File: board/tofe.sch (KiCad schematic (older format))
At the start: 6 parts, among them P301 TOFE-8X, U301 24AA01/24LC01B

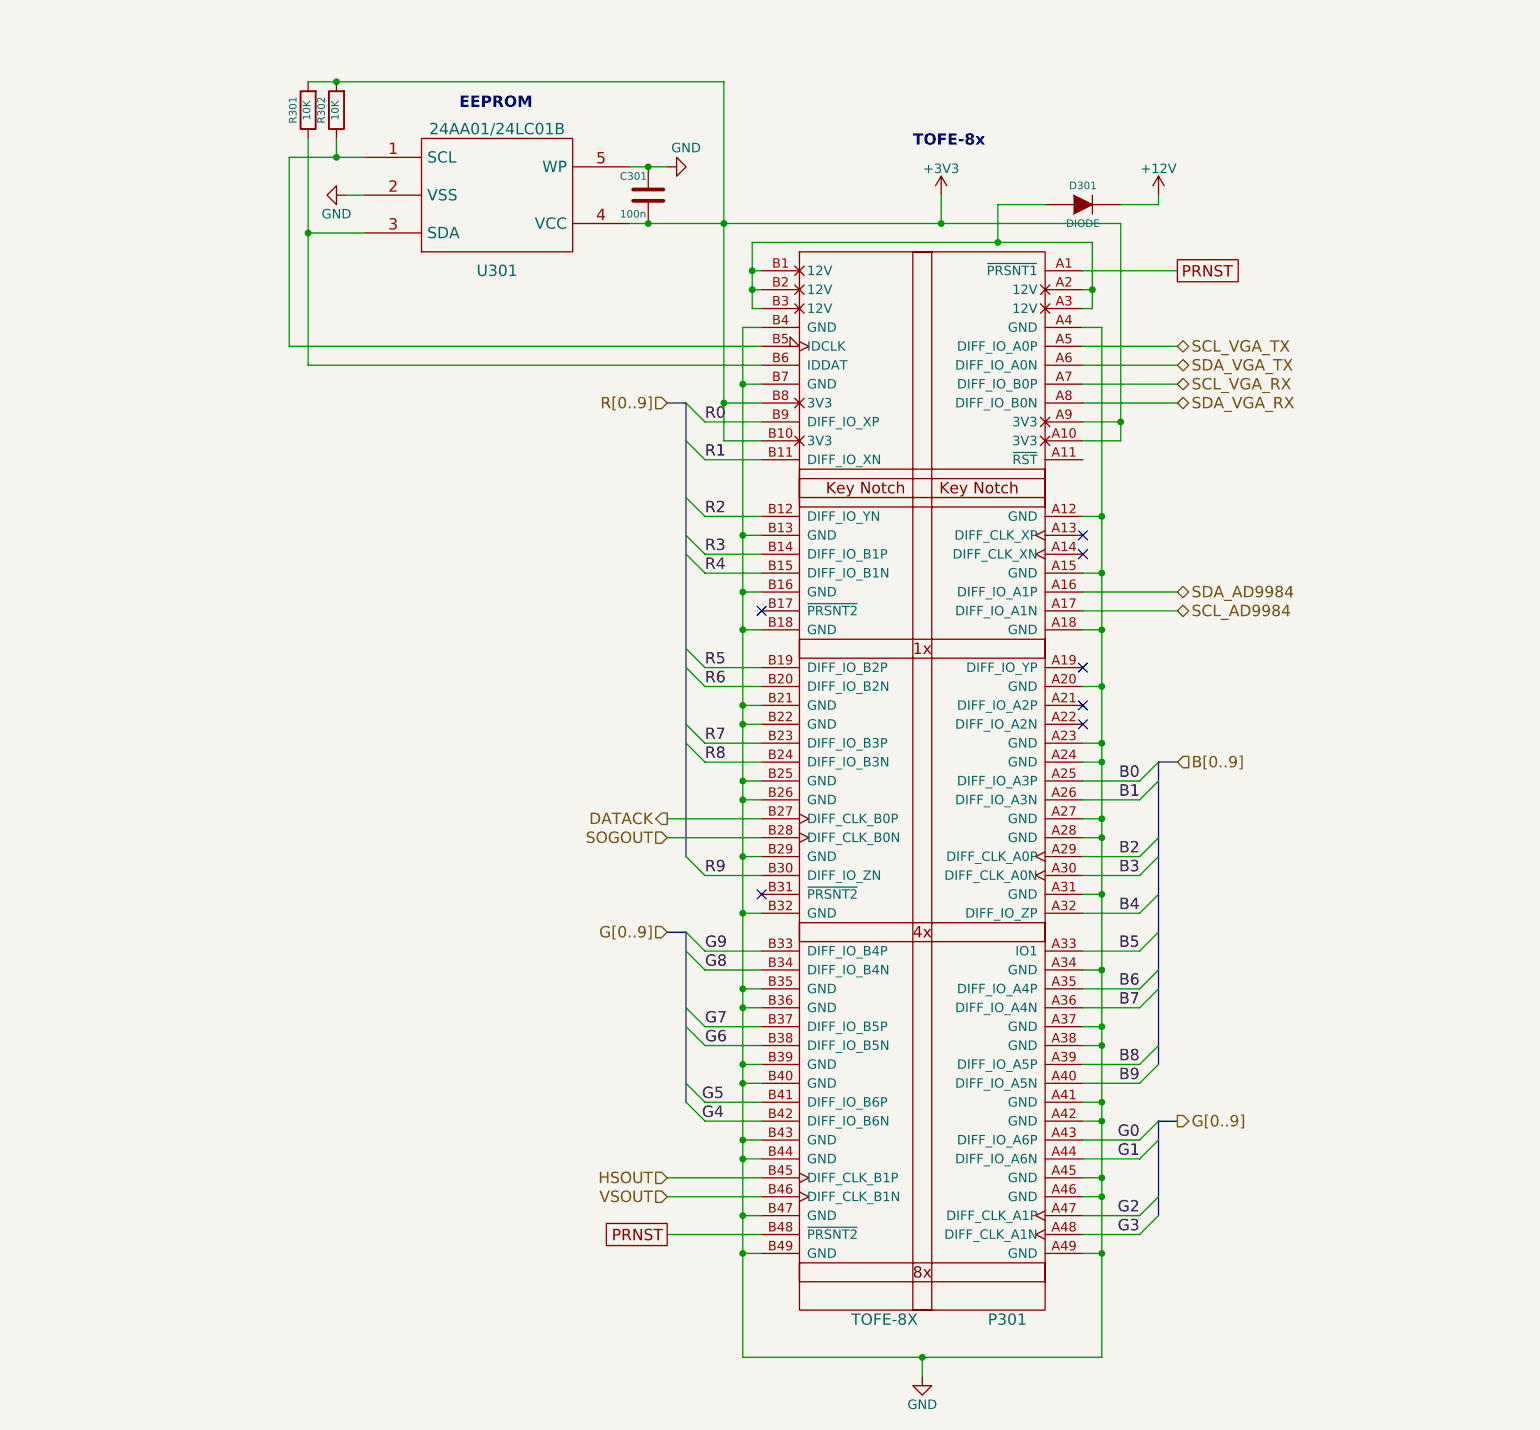
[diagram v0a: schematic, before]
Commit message: Add jumper for EEPROM WP and breakout unused pins to header that can jumper to LEDs
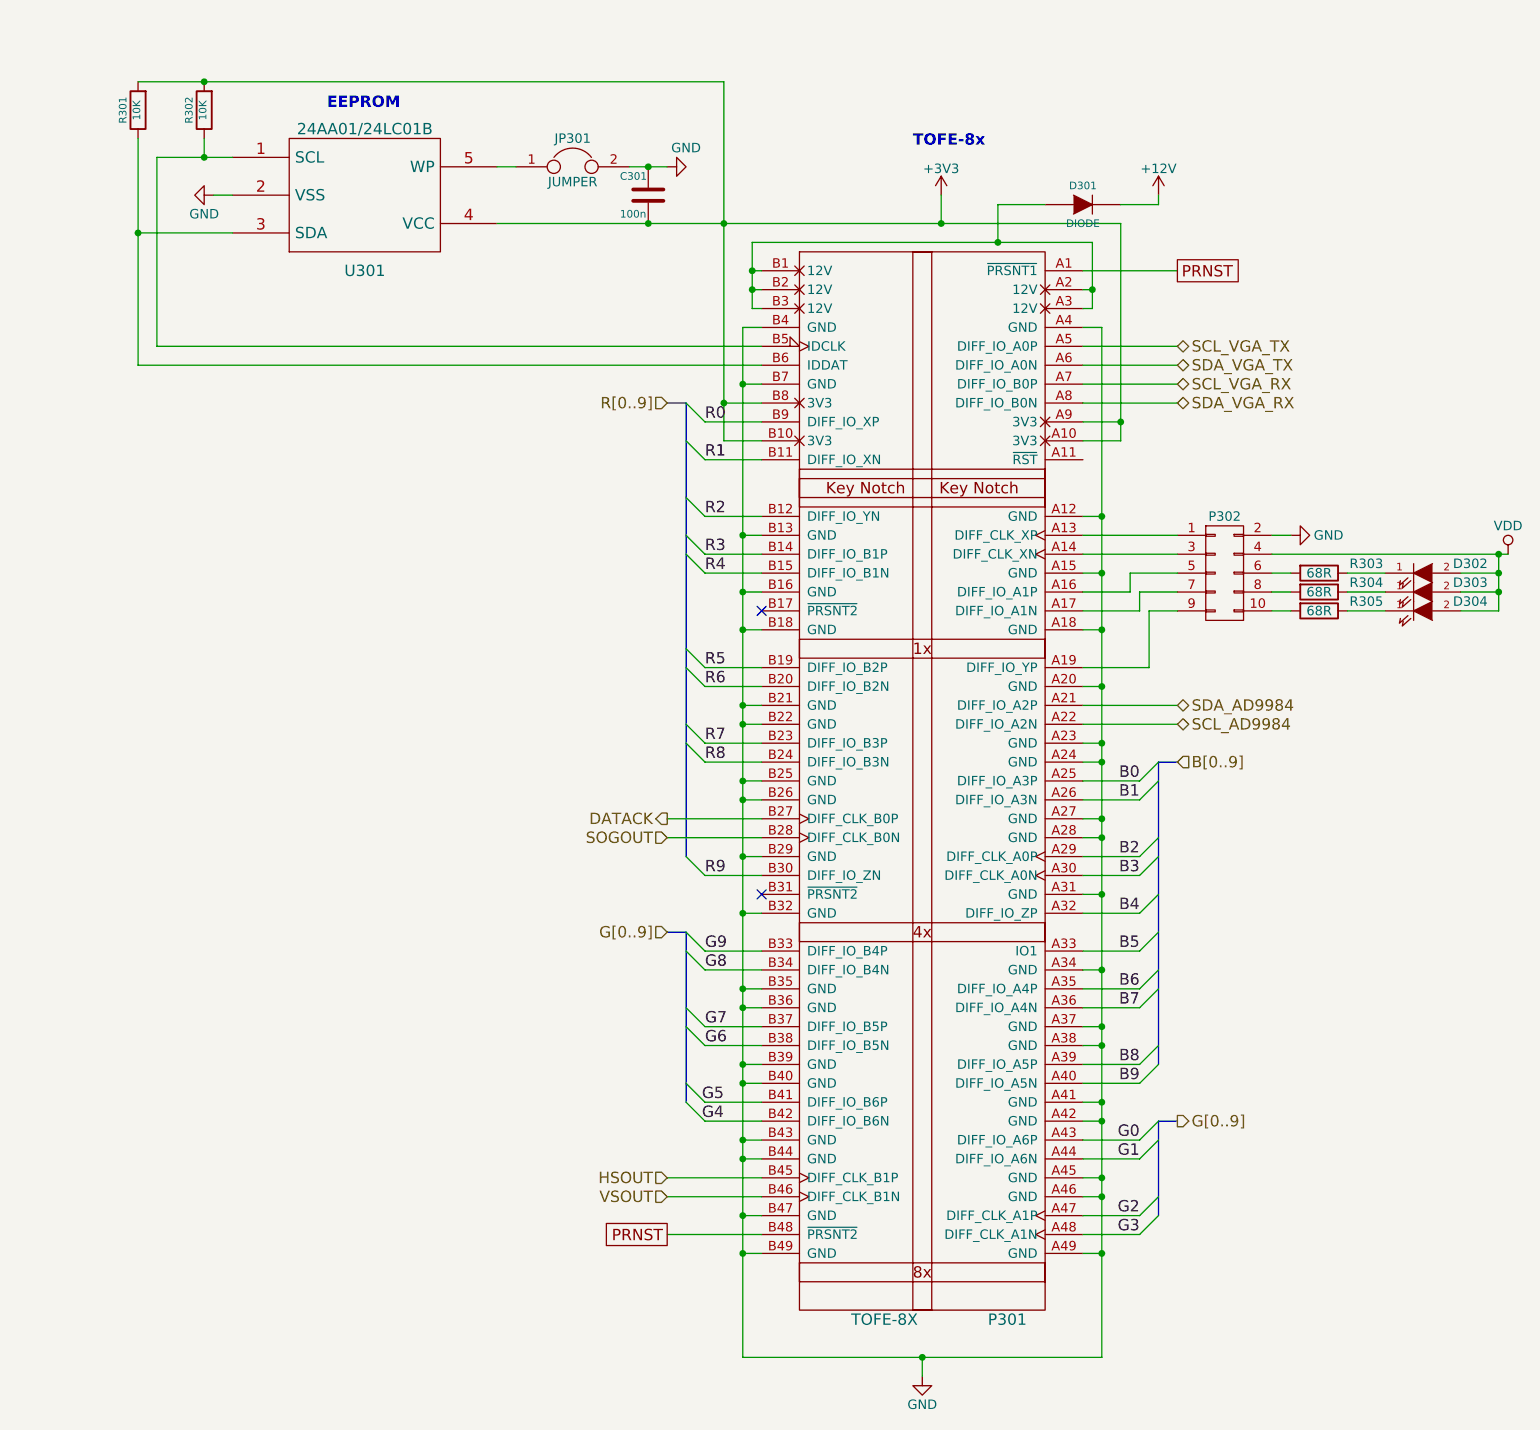
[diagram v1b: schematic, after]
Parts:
- added D302, D303, D304: LED, symbol LED
- added JP301: JUMPER, symbol JUMPER
- added P302: CONN_02X05, symbol CONN_02X05
- added R303, R304, R305: 68R, symbol R
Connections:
- net GND: now also JP301.2, P302.2 (P2); no longer U301.5 (WP)
- net SCL_AD9984: now also P301.A22 (DIFF_IO_A2N); no longer P301.A17 (DIFF_IO_A1N)
- net SDA_AD9984: now also P301.A21 (DIFF_IO_A2P); no longer P301.A16 (DIFF_IO_A1P)
- net at P301.A13 (DIFF_CLK_XP): now also P302.1 (P1)
- net at P301.A14 (DIFF_CLK_XN): now also P302.3 (P3)
- net at P301.A19 (DIFF_IO_YP): now also P302.9 (P9)
- new net: P301.A16 (DIFF_IO_A1P), P302.5 (P5)
- new net: P301.A17 (DIFF_IO_A1N), P302.7 (P7)
- new net: JP301.1, U301.5 (WP)
- new net: P302.10 (P10), R305.2
- new net: P302.6 (P6), R303.2
- new net: P302.8 (P8), R304.2
- new net: D302.1 (K), R303.1
- new net: D303.1 (K), R304.1
- new net: D304.1 (K), R305.1
- new net VDD: D302.2 (A), D303.2 (A), D304.2 (A), P302.4 (P4)
- no-connect marks 7 -> 2
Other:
- moved on the sheet: R301, R302, U301

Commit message: Add I2C headers
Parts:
- added P301: TOFE I2C, symbol CONN_01X04
- renumbered P301 to P302, P302 to P303
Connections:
- net +3V3: now also P301.1 (P1)
- net GND: now also P301.4 (P4)
- net at P302.B5 (IDCLK), R302.1, U301.1 (SCL): now also P301.2 (P2)
- net at P302.B6 (IDDAT), R301.1, U301.3 (SDA): now also P301.3 (P3)
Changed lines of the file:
@@
 $EndDescr
 $Comp
-L TOFE-8X P301
+L TOFE-8X P302
 U 1 1 561CABB0
 P 5900 4350
-F 0 "P301" H 5900 1500 60  0000 C CNN
+F 0 "P302" H 5900 1500 60  0000 C CNN
 F 1 "TOFE-8X" H 5250 1500 60  0000 C CNN
 F 2 "~" H 4600 4050 60  0000 C CNN
@@
 SDA_VGA_RX
 $Comp
-L GND #PWR303
+L GND #PWR304
 U 1 1 5641057B
 P 5450 7500
-F 0 "#PWR303" H 5450 7250 50  0001 C CNN
+F 0 "#PWR304" H 5450 7250 50  0001 C CNN
 F 1 "GND" H 5450 7350 50  0000 C CNN
 F 2 "" H 5450 7500 60  0000 C CNN
@@
 $EndComp
 $Comp
-L GND #PWR302
+L GND #PWR303
 U 1 1 56410719
 P 4100 1100
-F 0 "#PWR302" H 4100 850 50  0001 C CNN
+F 0 "#PWR303" H 4100 850 50  0001 C CNN
 F 1 "GND" V 4200 1000 50  0000 C CNN
 F 2 "" H 4100 1100 60  0000 C CNN
@@
 $EndComp
 $Comp
-L GND #PWR301
+L GND #PWR302
 U 1 1 564109C3
 P 1700 1250
-F 0 "#PWR301" H 1700 1000 50  0001 C CNN
+F 0 "#PWR302" H 1700 1000 50  0001 C CNN
 F 1 "GND" V 1800 1200 50  0000 C CNN
 F 2 "" H 1700 1250 60  0000 C CNN
@@
 $EndComp
 $Comp
-L +3V3 #PWR304
+L +3V3 #PWR305
 U 1 1 56412B64
 P 5550 1250
-F 0 "#PWR304" H 5550 1100 50  0001 C CNN
+F 0 "#PWR305" H 5550 1100 50  0001 C CNN
 F 1 "+3V3" H 5550 1390 50  0000 C CNN
 F 2 "" H 5550 1250 60  0000 C CNN
@@
 $EndComp
 $Comp
-L +12V #PWR305
+L +12V #PWR306
 U 1 1 56412B95
 P 6700 1250
-F 0 "#PWR305" H 6700 1100 50  0001 C CNN
+F 0 "#PWR306" H 6700 1100 50  0001 C CNN
 F 1 "+12V" H 6700 1390 50  0000 C CNN
 F 2 "" H 6700 1250 60  0000 C CNN
@@
 	1400 1050 1800 1050
 Wire Wire Line
-	1300 1450 1800 1450
+	1000 1450 1800 1450
 Connection ~ 4000 1100
 Wire Wire Line
@@
 Connection ~ 1650 1050
 Wire Wire Line
-	1300 650  4400 650
+	1100 650  4400 650
 Connection ~ 4400 1400
 Connection ~ 1650 650
@@
 Connection ~ 1300 1450
 $Comp
-L CONN_02X05 P302
+L CONN_02X05 P303
 U 1 1 56925815
 P 7050 3250
-F 0 "P302" H 7050 3550 50  0000 C CNN
+F 0 "P303" H 7050 3550 50  0000 C CNN
 F 1 "CONN_02X05" H 7050 2950 50  0001 C CNN
 F 2 "" H 7050 2050 50  0000 C CNN
@@
 	6650 3450 6800 3450
 $Comp
-L GND #PWR306
+L GND #PWR307
 U 1 1 56925C0A
 P 7400 3050
-F 0 "#PWR306" H 7400 2800 50  0001 C CNN
+F 0 "#PWR307" H 7400 2800 50  0001 C CNN
 F 1 "GND" V 7400 2850 50  0000 C CNN
 F 2 "" H 7400 3050 50  0000 C CNN
@@
 $EndComp
 $Comp
-L VDD #PWR307
+L VDD #PWR308
 U 1 1 56925C2E
 P 8550 3150
-F 0 "#PWR307" H 8550 3000 50  0001 C CNN
+F 0 "#PWR308" H 8550 3000 50  0001 C CNN
 F 1 "VDD" H 8550 3300 50  0000 C CNN
 F 2 "" H 8550 3150 50  0000 C CNN
@@
 Wire Wire Line
 	7300 3150 8550 3150
+$Comp
+L CONN_01X04 P301
+U 1 1 569310F0
+P 800 1400
+F 0 "P301" H 800 1650 50  0000 C CNN
+F 1 "TOFE I2C" V 900 1400 50  0000 C CNN
+F 2 "" H 800 1400 50  0000 C CNN
+F 3 "" H 800 1400 50  0000 C CNN
+	1    800  1400
+	-1   0    0    -1
+$EndComp
+Wire Wire Line
+	1100 650  1100 1250
+Wire Wire Line
+	1100 1250 1000 1250
+Connection ~ 1300 650
+Wire Wire Line
+	1000 1350 1400 1350
+Connection ~ 1400 1350
+$Comp
+L GND #PWR301
+U 1 1 56931407
+P 1100 1550
+F 0 "#PWR301" H 1100 1300 50  0001 C CNN
+F 1 "GND" V 1000 1500 50  0000 C CNN
+F 2 "" H 1100 1550 50  0000 C CNN
+F 3 "" H 1100 1550 50  0000 C CNN
+	1    1100 1550
+	0    -1   -1   0
+$EndComp
+Wire Wire Line
+	1000 1550 1100 1550
 $EndSCHEMATC

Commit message: Add pullup resistor to EEPROM WP
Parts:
- added R303: 10K, symbol R
- renumbered R303 to R304, R304 to R305, R305 to R306
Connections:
- net +3V3: now also R303.1
- net at JP301.1, U301.5 (WP): now also R303.2
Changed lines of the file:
@@
 $EndComp
 $Comp
-L R R303
+L R R304
 U 1 1 56925CE8
 P 7550 3250
-F 0 "R303" V 7500 3500 50  0000 C CNN
+F 0 "R304" V 7500 3500 50  0000 C CNN
 F 1 "68R" V 7550 3250 50  0000 C CNN
 F 2 "" V 7480 3250 50  0000 C CNN
@@
 $EndComp
 $Comp
-L R R304
+L R R305
 U 1 1 56925FCB
 P 7550 3350
-F 0 "R304" V 7500 3600 50  0000 C CNN
+F 0 "R305" V 7500 3600 50  0000 C CNN
 F 1 "68R" V 7550 3350 50  0000 C CNN
 F 2 "" V 7480 3350 50  0000 C CNN
@@
 $EndComp
 $Comp
-L R R305
+L R R306
 U 1 1 569261A1
 P 7550 3450
-F 0 "R305" V 7500 3700 50  0000 C CNN
+F 0 "R306" V 7500 3700 50  0000 C CNN
 F 1 "68R" V 7550 3450 50  0000 C CNN
 F 2 "" V 7480 3450 50  0000 C CNN
@@
 Wire Wire Line
 	1000 1550 1100 1550
+$Comp
+L R R303
+U 1 1 56934090
+P 3250 850
+F 0 "R303" V 3330 850 50  0000 C CNN
+F 1 "10K" V 3250 850 50  0000 C CNN
+F 2 "" V 3180 850 50  0000 C CNN
+F 3 "" H 3250 850 50  0000 C CNN
+	1    3250 850
+	1    0    0    -1
+$EndComp
+Wire Wire Line
+	3250 700  3250 650
+Connection ~ 3250 650
+Wire Wire Line
+	3250 1000 3250 1100
+Connection ~ 3250 1100
 $EndSCHEMATC

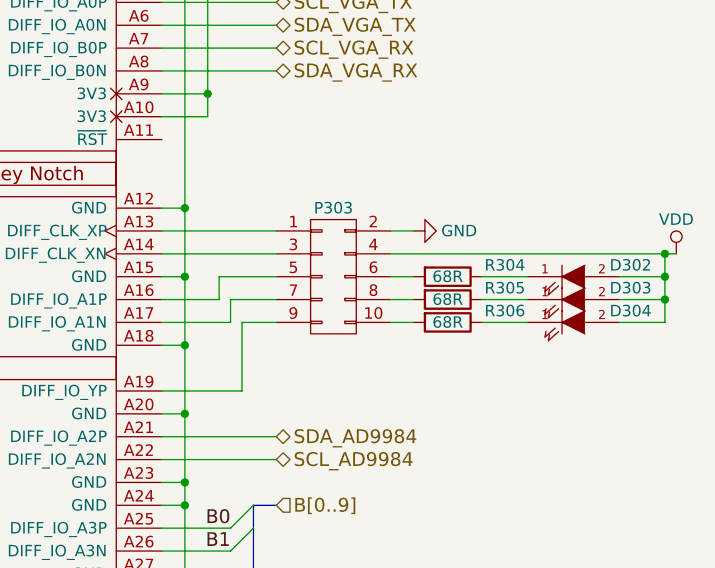
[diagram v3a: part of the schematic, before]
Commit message: Connect I2C level shifter EN to TOFE
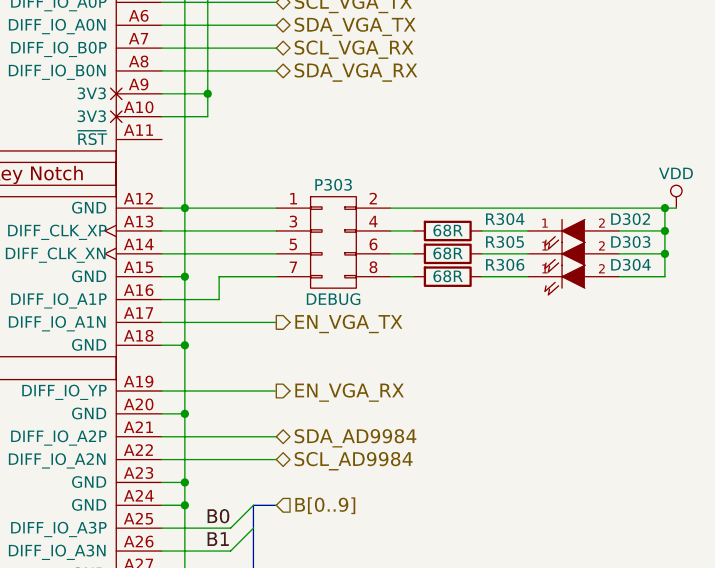
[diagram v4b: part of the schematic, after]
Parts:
- removed P303: CONN_02X05, symbol CONN_02X05
- added P303: DEBUG, symbol CONN_02X04
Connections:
- net GND: now also P303.1 (P1)
- net VDD: now also P303.2 (P2)
- net at P302.A13 (DIFF_CLK_XP): now also P303.3 (P3)
- net at P302.A14 (DIFF_CLK_XN): now also P303.5 (P5)
- net at P302.A16 (DIFF_IO_A1P): now also P303.7 (P7)
- net EN_VGA_TX: now reaches P302.A17 (DIFF_IO_A1N)
- net EN_VGA_RX: now reaches P302.A19 (DIFF_IO_YP)
- net at R306.2: now also P303.8 (P8)
- net at R304.2: now also P303.4 (P4)
- net at R305.2: now also P303.6 (P6)
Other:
- moved on the sheet: D302, D303, D304, R304, R305, R306
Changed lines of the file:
@@
 Connection ~ 5450 7400
 Wire Wire Line
-	6300 2950 6400 2950
+	6300 2950 6800 2950
 Connection ~ 6400 2950
 Wire Wire Line
@@
 	1300 950  1300 2150
 Connection ~ 1300 1450
-$Comp
-L CONN_02X05 P303
-U 1 1 56925815
-P 7050 3250
-F 0 "P303" H 7050 3550 50  0000 C CNN
-F 1 "CONN_02X05" H 7050 2950 50  0001 C CNN
-F 2 "" H 7050 2050 50  0000 C CNN
-F 3 "" H 7050 2050 50  0000 C CNN
-	1    7050 3250
-	1    0    0    -1
-$EndComp
 Wire Wire Line
 	6300 3050 6800 3050
@@
 Wire Wire Line
 	6550 3250 6800 3250
-Wire Wire Line
-	6300 3450 6600 3450
-Wire Wire Line
-	6600 3450 6600 3350
-Wire Wire Line
-	6600 3350 6800 3350
-Wire Wire Line
-	6300 3750 6650 3750
-Wire Wire Line
-	6650 3750 6650 3450
-Wire Wire Line
-	6650 3450 6800 3450
-$Comp
-L GND #PWR307
-U 1 1 56925C0A
-P 7400 3050
-F 0 "#PWR307" H 7400 2800 50  0001 C CNN
-F 1 "GND" V 7400 2850 50  0000 C CNN
-F 2 "" H 7400 3050 50  0000 C CNN
-F 3 "" H 7400 3050 50  0000 C CNN
-	1    7400 3050
-	0    -1   -1   0
-$EndComp
-$Comp
-L VDD #PWR308
+$Comp
+L VDD #PWR307
 U 1 1 56925C2E
-P 8550 3150
-F 0 "#PWR308" H 8550 3000 50  0001 C CNN
-F 1 "VDD" H 8550 3300 50  0000 C CNN
-F 2 "" H 8550 3150 50  0000 C CNN
-F 3 "" H 8550 3150 50  0000 C CNN
-	1    8550 3150
+P 8550 2950
+F 0 "#PWR307" H 8550 2800 50  0001 C CNN
+F 1 "VDD" H 8550 3100 50  0000 C CNN
+F 2 "" H 8550 2950 50  0000 C CNN
+F 3 "" H 8550 2950 50  0000 C CNN
+	1    8550 2950
 	1    0    0    -1
 $EndComp
@@
 L LED D302
 U 1 1 56925C52
+P 8100 3050
+F 0 "D302" H 8350 3100 50  0000 C CNN
+F 1 "LED" H 8100 2950 50  0001 C CNN
+F 2 "" H 8100 3050 50  0000 C CNN
+F 3 "" H 8100 3050 50  0000 C CNN
+	1    8100 3050
+	1    0    0    -1
+$EndComp
+$Comp
+L R R304
+U 1 1 56925CE8
+P 7550 3050
+F 0 "R304" V 7500 3300 50  0000 C CNN
+F 1 "68R" V 7550 3050 50  0000 C CNN
+F 2 "" V 7480 3050 50  0000 C CNN
+F 3 "" H 7550 3050 50  0000 C CNN
+	1    7550 3050
+	0    1    1    0
+$EndComp
+Wire Wire Line
+	7300 3050 7400 3050
+Wire Wire Line
+	7700 3050 7900 3050
+$Comp
+L LED D303
+U 1 1 56925FC5
+P 8100 3150
+F 0 "D303" H 8350 3200 50  0000 C CNN
+F 1 "LED" H 8100 3050 50  0001 C CNN
+F 2 "" H 8100 3150 50  0000 C CNN
+F 3 "" H 8100 3150 50  0000 C CNN
+	1    8100 3150
+	1    0    0    -1
+$EndComp
+$Comp
+L R R305
+U 1 1 56925FCB
+P 7550 3150
+F 0 "R305" V 7500 3400 50  0000 C CNN
+F 1 "68R" V 7550 3150 50  0000 C CNN
+F 2 "" V 7480 3150 50  0000 C CNN
+F 3 "" H 7550 3150 50  0000 C CNN
+	1    7550 3150
+	0    1    1    0
+$EndComp
+Wire Wire Line
+	7300 3150 7400 3150
+Wire Wire Line
+	7700 3150 7900 3150
+$Comp
+L LED D304
+U 1 1 5692619B
 P 8100 3250
-F 0 "D302" H 8350 3300 50  0000 C CNN
+F 0 "D304" H 8350 3300 50  0000 C CNN
 F 1 "LED" H 8100 3150 50  0001 C CNN
 F 2 "" H 8100 3250 50  0000 C CNN
@@
 $EndComp
 $Comp
-L R R304
-U 1 1 56925CE8
+L R R306
+U 1 1 569261A1
 P 7550 3250
-F 0 "R304" V 7500 3500 50  0000 C CNN
+F 0 "R306" V 7500 3500 50  0000 C CNN
 F 1 "68R" V 7550 3250 50  0000 C CNN
 F 2 "" V 7480 3250 50  0000 C CNN
@@
 Wire Wire Line
 	7700 3250 7900 3250
-$Comp
-L LED D303
-U 1 1 56925FC5
-P 8100 3350
-F 0 "D303" H 8350 3400 50  0000 C CNN
-F 1 "LED" H 8100 3250 50  0001 C CNN
-F 2 "" H 8100 3350 50  0000 C CNN
-F 3 "" H 8100 3350 50  0000 C CNN
-	1    8100 3350
-	1    0    0    -1
-$EndComp
-$Comp
-L R R305
-U 1 1 56925FCB
-P 7550 3350
-F 0 "R305" V 7500 3600 50  0000 C CNN
-F 1 "68R" V 7550 3350 50  0000 C CNN
-F 2 "" V 7480 3350 50  0000 C CNN
-F 3 "" H 7550 3350 50  0000 C CNN
-	1    7550 3350
-	0    1    1    0
-$EndComp
-Wire Wire Line
-	7300 3350 7400 3350
-Wire Wire Line
-	7700 3350 7900 3350
-$Comp
-L LED D304
-U 1 1 5692619B
-P 8100 3450
-F 0 "D304" H 8350 3500 50  0000 C CNN
-F 1 "LED" H 8100 3350 50  0001 C CNN
-F 2 "" H 8100 3450 50  0000 C CNN
-F 3 "" H 8100 3450 50  0000 C CNN
-	1    8100 3450
-	1    0    0    -1
-$EndComp
-$Comp
-L R R306
-U 1 1 569261A1
-P 7550 3450
-F 0 "R306" V 7500 3700 50  0000 C CNN
-F 1 "68R" V 7550 3450 50  0000 C CNN
-F 2 "" V 7480 3450 50  0000 C CNN
-F 3 "" H 7550 3450 50  0000 C CNN
-	1    7550 3450
-	0    1    1    0
-$EndComp
-Wire Wire Line
-	7300 3450 7400 3450
-Wire Wire Line
-	7700 3450 7900 3450
-Wire Wire Line
-	7300 3050 7400 3050
+Wire Wire Line
+	8300 3050 8500 3050
+Wire Wire Line
+	8500 3250 8500 2950
+Connection ~ 8500 2950
+Wire Wire Line
+	8300 3150 8500 3150
+Connection ~ 8500 3050
 Wire Wire Line
 	8300 3250 8500 3250
-Wire Wire Line
-	8500 3450 8500 3150
 Connection ~ 8500 3150
 Wire Wire Line
-	8300 3350 8500 3350
-Connection ~ 8500 3250
-Wire Wire Line
-	8300 3450 8500 3450
-Connection ~ 8500 3350
-Wire Wire Line
-	7300 3150 8550 3150
+	7300 2950 8550 2950
 $Comp
 L CONN_01X04 P301
@@
 	3250 1000 3250 1100
 Connection ~ 3250 1100
+$Comp
+L CONN_02X04 P303
+U 1 1 569346A3
+P 7050 3100
+F 0 "P303" H 7050 3350 50  0000 C CNN
+F 1 "DEBUG" H 7050 2850 50  0000 C CNN
+F 2 "" H 7050 1900 50  0000 C CNN
+F 3 "" H 7050 1900 50  0000 C CNN
+	1    7050 3100
+	1    0    0    -1
+$EndComp
+Text HLabel 6800 3450 2    60   Output ~ 0
+EN_VGA_TX
+Text HLabel 6800 3750 2    60   Output ~ 0
+EN_VGA_RX
+Wire Wire Line
+	6300 3450 6800 3450
+Wire Wire Line
+	6300 3750 6800 3750
 $EndSCHEMATC
